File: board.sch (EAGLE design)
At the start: 47 parts, among them U1 MAX232

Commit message: added gitignore, tweaked board
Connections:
- removed net N$2: U1.R1OUT
- removed net N$20: U1.R2OUT
- removed net N$21: U1.T2IN
- removed net N$9: U1.T1IN
- net PC2: now also U1.R1OUT
- net PC3: now also U1.T1IN
- net PC6: now also U1.R2OUT
- net PC7: now also U1.T2IN
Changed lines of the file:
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@@
 </segment>
 </net>
-<net name="N$2" class="0">
+<net name="PC2" class="0">
 <segment>
 <pinref part="U1" gate="G$1" pin="R1OUT"/>
@@
 </segment>
 </net>
-<net name="N$9" class="0">
+<net name="PC3" class="0">
 <segment>
 <pinref part="U1" gate="G$1" pin="T1IN"/>
@@
 </segment>
 </net>
-<net name="N$20" class="0">
+<net name="PC6" class="0">
 <segment>
 <pinref part="U1" gate="G$1" pin="R2OUT"/>
 <wire x1="48.26" y1="45.72" x2="45.72" y2="45.72" width="0" layer="91"/>
 <label x="45.72" y="45.72" size="1.778" layer="95" rot="R180"/>
-</segment>
-</net>
-<net name="N$21" class="0">
-<segment>
-<pinref part="U1" gate="G$1" pin="T2IN"/>
-<wire x1="48.26" y1="50.8" x2="45.72" y2="50.8" width="0" layer="91"/>
-<label x="45.72" y="50.8" size="1.778" layer="95" rot="R180"/>
 </segment>
 </net>
@@
 </segment>
 </net>
+<net name="PC7" class="0">
+<segment>
+<pinref part="U1" gate="G$1" pin="T2IN"/>
+<wire x1="48.26" y1="50.8" x2="45.72" y2="50.8" width="0" layer="91"/>
+<label x="45.72" y="50.8" size="1.778" layer="95" rot="R180"/>
+</segment>
+</net>

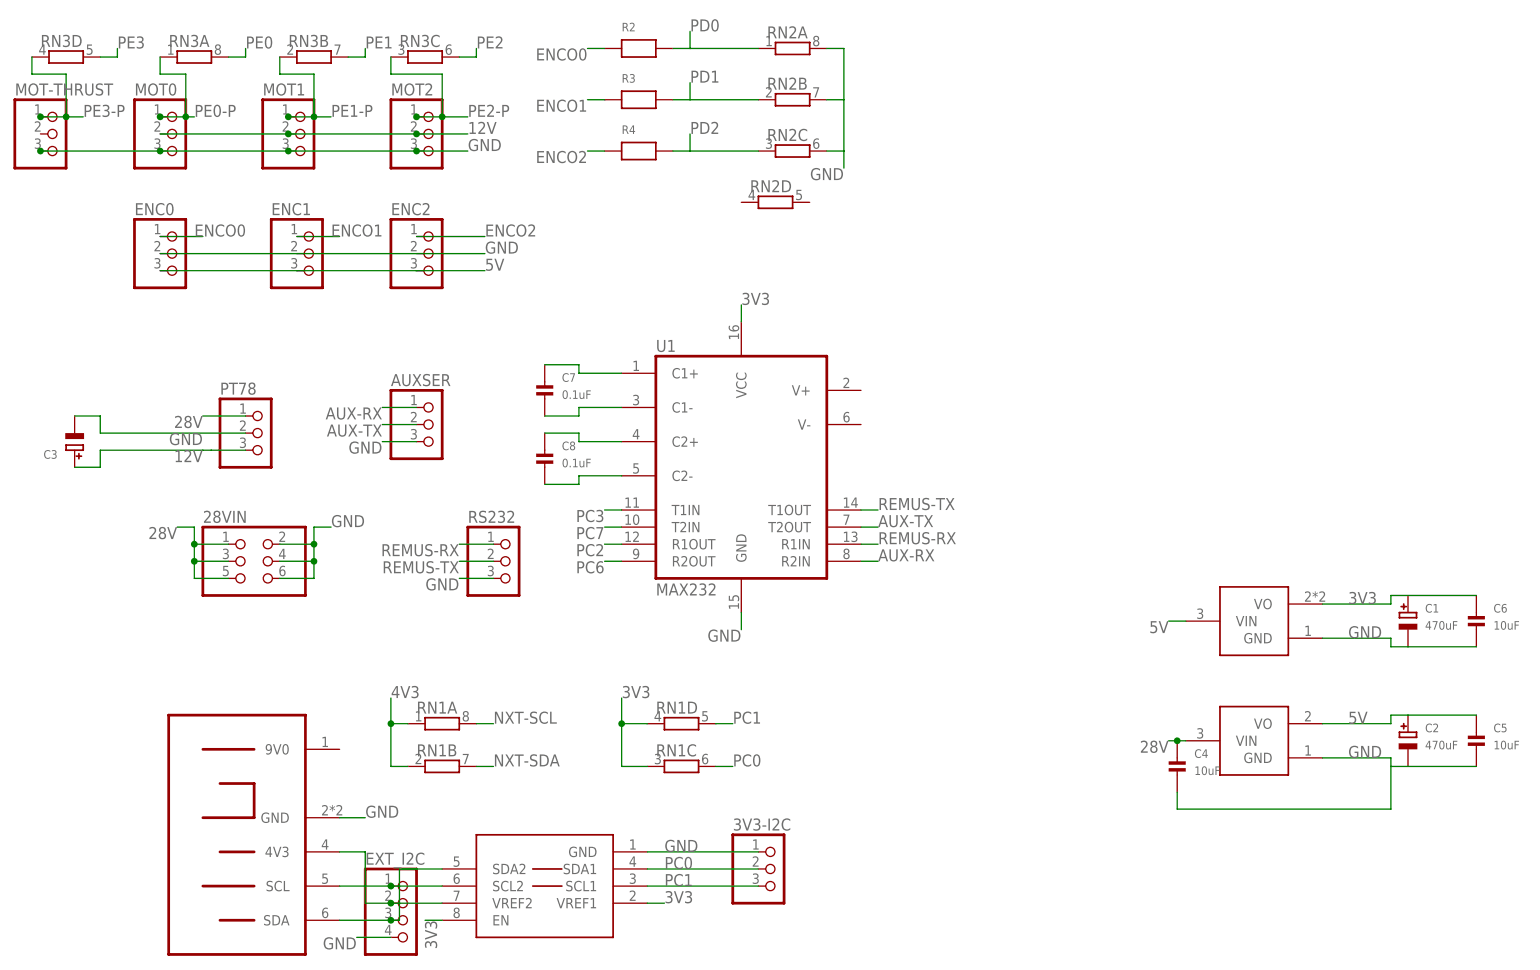
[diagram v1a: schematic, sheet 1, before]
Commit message: add some part values, nudge some traces
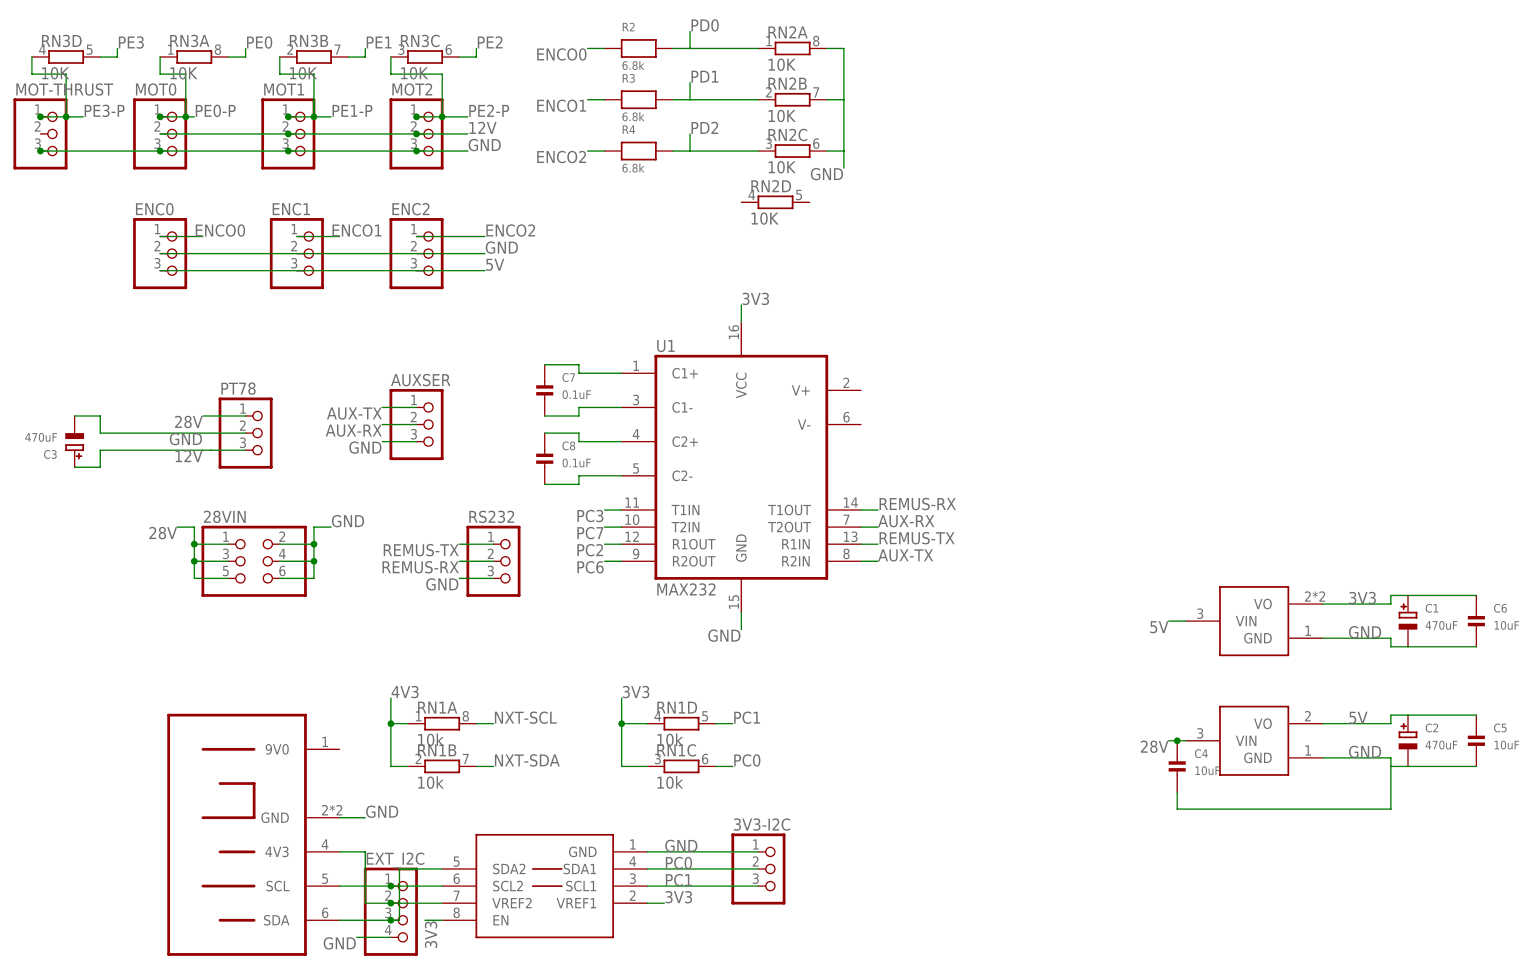
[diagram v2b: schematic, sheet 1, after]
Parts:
- C10, C9: value (none) -> 0.1uF
- C11: value (none) -> 18pF
- C12: value (none) -> 10pF
- C13, C14: value (none) -> 1uF
- C3: value (none) -> 470uF
- R1: value (none) -> 130O
- R2, R3, R4: value (none) -> 6.8k
- RN1: value (none) -> 10k
- RN2, RN3: value (none) -> 10K
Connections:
- net AUX-RX: now also AUXSER.2, U1.T2OUT; no longer AUXSER.1, U1.R2IN
- net AUX-TX: now also AUXSER.1, U1.R2IN; no longer AUXSER.2, U1.T2OUT
- net REMUS-RX: now also RS232.2, U1.T1OUT; no longer RS232.1, U1.R1IN
- net REMUS-TX: now also RS232.1, U1.R1IN; no longer RS232.2, U1.T1OUT
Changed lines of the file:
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@@
 <part name="U$1" library="nonolith" deviceset="PCA9306" device=""/>
 <part name="U1" library="nonolith" deviceset="MAX232" device=""/>
-<part name="RN1" library="nonolith" deviceset="RNETWORK" device=""/>
+<part name="RN1" library="nonolith" deviceset="RNETWORK" device="" value="10k"/>
 <part name="U$2" library="nonolith" deviceset="NXT-CONNECTOR" device=""/>
 <part name="PT78" library="nonolith" deviceset="HEADER-1X3" device="ROUND"/>
@@
 <part name="C1" library="microbuilder" deviceset="CAP_TANTALUM" device="D/7343_WAVE" value="470uF"/>
 <part name="C2" library="microbuilder" deviceset="CAP_TANTALUM" device="D/7343_WAVE" value="470uF"/>
-<part name="C3" library="microbuilder" deviceset="CAP_TANTALUM" device="D/7343_WAVE"/>
+<part name="C3" library="microbuilder" deviceset="CAP_TANTALUM" device="D/7343_WAVE" value="470uF"/>
 <part name="C4" library="nonolith" deviceset="CAP_CERAMIC" device="1206" value="10uF"/>
 <part name="C5" library="nonolith" deviceset="CAP_CERAMIC" device="1206" value="10uF"/>
@@
 <part name="U$6" library="SparkFun" deviceset="M19" device=""/>
 <part name="U$7" library="SparkFun" deviceset="M19" device=""/>
-<part name="C9" library="nonolith" deviceset="CAP_CERAMIC" device="0603"/>
-<part name="C10" library="nonolith" deviceset="CAP_CERAMIC" device="0603"/>
+<part name="C9" library="nonolith" deviceset="CAP_CERAMIC" device="0603" value="0.1uF"/>
+<part name="C10" library="nonolith" deviceset="CAP_CERAMIC" device="0603" value="0.1uF"/>
 <part name="CN1" library="nonolith" deviceset="USB" device="MICROB"/>
 <part name="JP1" library="nonolith" deviceset="HEADER-2X3" device=""/>
 <part name="Y1" library="nonolith" deviceset="CRYSTAL" device=""/>
-<part name="C11" library="nonolith" deviceset="CAP_CERAMIC" device="0603"/>
-<part name="C12" library="nonolith" deviceset="CAP_CERAMIC" device="0603"/>
+<part name="C11" library="nonolith" deviceset="CAP_CERAMIC" device="0603" value="18pF"/>
+<part name="C12" library="nonolith" deviceset="CAP_CERAMIC" device="0603" value="10pF"/>
 <part name="LED1" library="microbuilder" deviceset="LED" device="0603"/>
 <part name="U$8" library="nonolith" deviceset="GND" device=""/>
 <part name="U$9" library="nonolith" deviceset="GND" device=""/>
 <part name="U$10" library="nonolith" deviceset="GND" device=""/>
-<part name="R1" library="nonolith" deviceset="RESISTOR" device="0603"/>
-<part name="C13" library="nonolith" deviceset="CAP_CERAMIC" device="0603"/>
-<part name="C14" library="nonolith" deviceset="CAP_CERAMIC" device="0603"/>
-<part name="RN2" library="nonolith" deviceset="RNETWORK" device=""/>
-<part name="R2" library="nonolith" deviceset="RESISTOR" device="0603"/>
-<part name="R3" library="nonolith" deviceset="RESISTOR" device="0603"/>
-<part name="R4" library="nonolith" deviceset="RESISTOR" device="0603"/>
+<part name="R1" library="nonolith" deviceset="RESISTOR" device="0603" value="130O"/>
+<part name="C13" library="nonolith" deviceset="CAP_CERAMIC" device="0603" value="1uF"/>
+<part name="C14" library="nonolith" deviceset="CAP_CERAMIC" device="0603" value="1uF"/>
+<part name="RN2" library="nonolith" deviceset="RNETWORK" device="" value="10K"/>
+<part name="R2" library="nonolith" deviceset="RESISTOR" device="0603" value="6.8k"/>
+<part name="R3" library="nonolith" deviceset="RESISTOR" device="0603" value="6.8k"/>
+<part name="R4" library="nonolith" deviceset="RESISTOR" device="0603" value="6.8k"/>
 <part name="AUXSER" library="nonolith" deviceset="HEADER-1X3" device="ROUND"/>
 <part name="MOT-THRUST" library="nonolith" deviceset="HEADER-1X3" device="ROUND"/>
 <part name="3V3-I2C" library="nonolith" deviceset="HEADER-1X3" device="ROUND"/>
 <part name="EXT_I2C" library="nonolith" deviceset="HEADER-1X4" device="ROUND"/>
-<part name="RN3" library="nonolith" deviceset="RNETWORK" device=""/>
+<part name="RN3" library="nonolith" deviceset="RNETWORK" device="" value="10K"/>
 </parts>
 <sheets>
@@
 <net name="REMUS-RX" class="0">
 <segment>
+<pinref part="U1" gate="G$1" pin="T1OUT"/>
+<wire x1="83.82" y1="53.34" x2="86.36" y2="53.34" width="0" layer="91"/>
+<label x="86.36" y="53.34" size="1.778" layer="95"/>
+</segment>
+<segment>
+<pinref part="RS232" gate="A" pin="2"/>
+<wire x1="29.21" y1="45.72" x2="24.13" y2="45.72" width="0" layer="91"/>
+<label x="24.13" y="45.72" size="1.778" layer="95" rot="R180"/>
+</segment>
+</net>
+<net name="REMUS-TX" class="0">
+<segment>
+<pinref part="U1" gate="G$1" pin="R1IN"/>
+<wire x1="83.82" y1="48.26" x2="86.36" y2="48.26" width="0" layer="91"/>
+<label x="86.36" y="48.26" size="1.778" layer="95"/>
+</segment>
+<segment>
 <pinref part="RS232" gate="A" pin="1"/>
 <wire x1="29.21" y1="48.26" x2="24.13" y2="48.26" width="0" layer="91"/>
 <label x="24.13" y="48.26" size="1.778" layer="95" rot="R180"/>
-</segment>
-<segment>
-<pinref part="U1" gate="G$1" pin="R1IN"/>
-<wire x1="83.82" y1="48.26" x2="86.36" y2="48.26" width="0" layer="91"/>
-<label x="86.36" y="48.26" size="1.778" layer="95"/>
-</segment>
-</net>
-<net name="REMUS-TX" class="0">
-<segment>
-<pinref part="RS232" gate="A" pin="2"/>
-<wire x1="29.21" y1="45.72" x2="24.13" y2="45.72" width="0" layer="91"/>
-<label x="24.13" y="45.72" size="1.778" layer="95" rot="R180"/>
-</segment>
-<segment>
-<pinref part="U1" gate="G$1" pin="T1OUT"/>
-<wire x1="83.82" y1="53.34" x2="86.36" y2="53.34" width="0" layer="91"/>
-<label x="86.36" y="53.34" size="1.778" layer="95"/>
 </segment>
 </net>
@@
 <net name="AUX-TX" class="0">
 <segment>
+<pinref part="U1" gate="G$1" pin="R2IN"/>
+<wire x1="83.82" y1="45.72" x2="86.36" y2="45.72" width="0" layer="91"/>
+<label x="86.36" y="45.72" size="1.778" layer="95"/>
+</segment>
+<segment>
+<pinref part="AUXSER" gate="A" pin="1"/>
+<wire x1="17.78" y1="68.58" x2="12.7" y2="68.58" width="0" layer="91"/>
+<label x="12.7" y="68.58" size="1.778" layer="95" rot="R180"/>
+</segment>
+</net>
+<net name="AUX-RX" class="0">
+<segment>
+<pinref part="U1" gate="G$1" pin="T2OUT"/>
+<wire x1="83.82" y1="50.8" x2="86.36" y2="50.8" width="0" layer="91"/>
+<label x="86.36" y="50.8" size="1.778" layer="95"/>
+</segment>
+<segment>
 <pinref part="AUXSER" gate="A" pin="2"/>
 <wire x1="17.78" y1="66.04" x2="12.7" y2="66.04" width="0" layer="91"/>
 <label x="12.7" y="66.04" size="1.778" layer="95" rot="R180"/>
 </segment>
-<segment>
-<pinref part="U1" gate="G$1" pin="T2OUT"/>
-<wire x1="83.82" y1="50.8" x2="86.36" y2="50.8" width="0" layer="91"/>
-<label x="86.36" y="50.8" size="1.778" layer="95"/>
-</segment>
-</net>
-<net name="AUX-RX" class="0">
-<segment>
-<pinref part="U1" gate="G$1" pin="R2IN"/>
-<wire x1="83.82" y1="45.72" x2="86.36" y2="45.72" width="0" layer="91"/>
-<label x="86.36" y="45.72" size="1.778" layer="95"/>
-</segment>
-<segment>
-<pinref part="AUXSER" gate="A" pin="1"/>
-<wire x1="17.78" y1="68.58" x2="12.7" y2="68.58" width="0" layer="91"/>
-<label x="12.7" y="68.58" size="1.778" layer="95" rot="R180"/>
-</segment>
-</net>
+</net>
